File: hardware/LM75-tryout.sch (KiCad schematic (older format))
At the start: 4 parts, among them J1 LM75_HEADER, U1 LM75

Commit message: update,
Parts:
- added JP1: EN, Jumper:SolderJumper-2_P1.3mm_Open_RoundedPad1.0x1.5mm, symbol Jumper:SolderJumper_2_Open
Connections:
- net +3V3: now also JP1.1 (A); no longer C1.1, RN1.6 (R3.2), RN1.7 (R2.2), RN1.8 (R1.2), U1.8 (VCC)
- new net: C1.1, JP1.2 (B), RN1.6 (R3.2), RN1.7 (R2.2), RN1.8 (R1.2), U1.8 (VCC)
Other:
- moved on the sheet: C1, J1, RN1, U1
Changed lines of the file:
@@
 EESchema Schematic File Version 4
+LIBS:LM75-tryout-cache
 EELAYER 29 0
 EELAYER END
@@
 L taobao-components:LM75 U1
 U 1 1 5CEF6143
-P 3000 2000
-F 0 "U1" H 3000 2450 50  0000 C CNN
-F 1 "LM75" H 3000 2350 50  0000 C CNN
-F 2 "Package_SO:SOP-8_3.76x4.96mm_P1.27mm" H 3000 1400 50  0001 C CNN
-F 3 "" H 3000 2000 50  0001 C CNN
-	1    3000 2000
+P 3850 2650
+F 0 "U1" H 3850 3100 50  0000 C CNN
+F 1 "LM75" H 3850 3000 50  0000 C CNN
+F 2 "Package_SO:SOP-8_3.76x4.96mm_P1.27mm" H 3850 2050 50  0001 C CNN
+F 3 "" H 3850 2650 50  0001 C CNN
+	1    3850 2650
 	1    0    0    -1
 $EndComp
@@
 L taobao-rpack:RN_472,0603 RN1
 U 1 1 5CEF7694
-P 2000 1450
-F 0 "RN1" H 2200 1500 50  0000 L CNN
-F 1 "RN_472,0603" H 2200 1450 50  0000 L CNN
-F 2 "Resistor_SMD:R_Array_Concave_4x0603" V 2275 1450 50  0001 C CNN
-F 3 "~" H 2000 1450 50  0001 C CNN
-	1    2000 1450
+P 2850 2100
+F 0 "RN1" H 3050 2150 50  0000 L CNN
+F 1 "RN_472,0603" H 3050 2100 50  0000 L CNN
+F 2 "Resistor_SMD:R_Array_Concave_4x0603" V 3125 2100 50  0001 C CNN
+F 3 "~" H 2850 2100 50  0001 C CNN
+	1    2850 2100
 	1    0    0    -1
 $EndComp
@@
 L taobao-c:C103,0603 C1
 U 1 1 5CEF7ED4
-P 4050 1450
-F 0 "C1" H 4150 1500 50  0000 L CNN
-F 1 "C103,0603" H 4150 1450 50  0000 L CNN
-F 2 "Capacitor_SMD:C_0603_1608Metric_Pad1.05x0.95mm_HandSolder" H 4050 1450 50  0001 C CNN
-F 3 "~" H 4050 1450 50  0001 C CNN
-	1    4050 1450
+P 4900 2100
+F 0 "C1" H 5000 2150 50  0000 L CNN
+F 1 "C103,0603" H 5000 2100 50  0000 L CNN
+F 2 "Capacitor_SMD:C_0603_1608Metric_Pad1.05x0.95mm_HandSolder" H 4900 2100 50  0001 C CNN
+F 3 "~" H 4900 2100 50  0001 C CNN
+	1    4900 2100
 	1    0    0    -1
 $EndComp
@@
 L power:GND #PWR0101
 U 1 1 5CEF86F3
-P 3650 2350
-F 0 "#PWR0101" H 3650 2100 50  0001 C CNN
-F 1 "GND" H 3700 2150 50  0000 C CNN
-F 2 "" H 3650 2350 50  0001 C CNN
-F 3 "" H 3650 2350 50  0001 C CNN
-	1    3650 2350
+P 4500 3000
+F 0 "#PWR0101" H 4500 2750 50  0001 C CNN
+F 1 "GND" H 4550 2800 50  0000 C CNN
+F 2 "" H 4500 3000 50  0001 C CNN
+F 3 "" H 4500 3000 50  0001 C CNN
+	1    4500 3000
 	1    0    0    -1
 $EndComp
 Wire Wire Line
-	3400 1950 3650 1950
+	4250 2600 4500 2600
 Wire Wire Line
-	3650 1950 3650 2050
+	4500 2600 4500 2700
 Wire Wire Line
-	3400 2050 3650 2050
-Connection ~ 3650 2050
+	4250 2700 4500 2700
+Connection ~ 4500 2700
 Wire Wire Line
-	3650 2050 3650 2150
+	4500 2700 4500 2800
 Wire Wire Line
-	3400 2150 3650 2150
-Connection ~ 3650 2150
+	4250 2800 4500 2800
+Connection ~ 4500 2800
 Wire Wire Line
-	3650 2150 3650 2350
+	4500 2800 4500 3000
 $Comp
 L power:GND #PWR0102
 U 1 1 5CEF9E27
-P 4050 1700
-F 0 "#PWR0102" H 4050 1450 50  0001 C CNN
-F 1 "GND" H 4100 1500 50  0000 C CNN
-F 2 "" H 4050 1700 50  0001 C CNN
-F 3 "" H 4050 1700 50  0001 C CNN
-	1    4050 1700
+P 4900 2350
+F 0 "#PWR0102" H 4900 2100 50  0001 C CNN
+F 1 "GND" H 4950 2150 50  0000 C CNN
+F 2 "" H 4900 2350 50  0001 C CNN
+F 3 "" H 4900 2350 50  0001 C CNN
+	1    4900 2350
 	1    0    0    -1
 $EndComp
 Wire Wire Line
-	4050 1550 4050 1700
+	4900 2200 4900 2350
 $Comp
 L power:+3V3 #PWR0103
 U 1 1 5CEFBBD2
-P 3350 1050
-F 0 "#PWR0103" H 3350 900 50  0001 C CNN
-F 1 "+3V3" H 3400 1250 50  0000 C CNN
-F 2 "" H 3350 1050 50  0001 C CNN
-F 3 "" H 3350 1050 50  0001 C CNN
-	1    3350 1050
+P 4200 1200
+F 0 "#PWR0103" H 4200 1050 50  0001 C CNN
+F 1 "+3V3" H 4250 1400 50  0000 C CNN
+F 2 "" H 4200 1200 50  0001 C CNN
+F 3 "" H 4200 1200 50  0001 C CNN
+	1    4200 1200
 	1    0    0    -1
 $EndComp
 Wire Wire Line
-	1800 1100 1800 1250
+	2650 1750 2650 1900
 Wire Wire Line
-	1800 1100 1900 1100
+	2650 1750 2750 1750
 Wire Wire Line
-	3350 1050 3350 1100
+	2750 1900 2750 1750
+Connection ~ 2750 1750
 Wire Wire Line
-	1900 1250 1900 1100
-Connection ~ 1900 1100
+	2750 1750 2850 1750
 Wire Wire Line
-	1900 1100 2000 1100
+	2850 1750 2850 1900
+Connection ~ 2850 1750
 Wire Wire Line
-	2000 1100 2000 1250
-Connection ~ 2000 1100
+	2850 1750 4200 1750
 Wire Wire Line
-	2000 1100 3350 1100
+	4900 2000 4900 1750
+Connection ~ 4200 1750
 Wire Wire Line
-	4050 1350 4050 1100
-Connection ~ 3350 1100
+	4200 1750 4400 1750
 Wire Wire Line
-	3350 1100 3550 1100
+	4250 2500 4400 2500
 Wire Wire Line
-	3400 1850 3550 1850
+	4400 2500 4400 1750
+Connection ~ 4400 1750
 Wire Wire Line
-	3550 1850 3550 1100
-Connection ~ 3550 1100
+	4400 1750 4900 1750
 Wire Wire Line
-	3550 1100 4050 1100
+	3450 2500 2650 2500
 Wire Wire Line
-	2600 1850 1800 1850
+	2650 2300 2650 2500
+Connection ~ 2650 2500
 Wire Wire Line
-	1800 1650 1800 1850
-Connection ~ 1800 1850
+	2650 2500 1800 2500
 Wire Wire Line
-	1800 1850 950  1850
+	1800 2600 2750 2600
 Wire Wire Line
-	950  1950 1900 1950
+	2750 2300 2750 2600
+Connection ~ 2750 2600
 Wire Wire Line
-	1900 1650 1900 1950
-Connection ~ 1900 1950
+	2750 2600 3450 2600
 Wire Wire Line
-	1900 1950 2600 1950
+	1800 2700 2850 2700
 Wire Wire Line
-	950  2050 2000 2050
+	2850 2300 2850 2700
+Connection ~ 2850 2700
 Wire Wire Line
-	2000 1650 2000 2050
-Connection ~ 2000 2050
-Wire Wire Line
-	2000 2050 2600 2050
+	2850 2700 3450 2700
 $Comp
 L power:GND #PWR0104
 U 1 1 5CF0201D
-P 2500 2350
-F 0 "#PWR0104" H 2500 2100 50  0001 C CNN
-F 1 "GND" H 2550 2150 50  0000 C CNN
-F 2 "" H 2500 2350 50  0001 C CNN
-F 3 "" H 2500 2350 50  0001 C CNN
-	1    2500 2350
+P 3350 3000
+F 0 "#PWR0104" H 3350 2750 50  0001 C CNN
+F 1 "GND" H 3400 2800 50  0000 C CNN
+F 2 "" H 3350 3000 50  0001 C CNN
+F 3 "" H 3350 3000 50  0001 C CNN
+	1    3350 3000
 	1    0    0    -1
 $EndComp
 Wire Wire Line
-	2500 2350 2500 2150
+	3350 3000 3350 2800
 Wire Wire Line
-	2500 2150 2600 2150
+	3350 2800 3450 2800
 $Comp
 L Connector:Conn_01x05_Female J1
 U 1 1 5CF06FB7
-P 750 1850
-F 0 "J1" H 600 2250 50  0000 C CNN
-F 1 "LM75_HEADER" H 600 2150 50  0000 C CNN
-F 2 "Connector_PinHeader_1.27mm:PinHeader_1x05_P1.27mm_Vertical" H 750 1850 50  0001 C CNN
-F 3 "~" H 750 1850 50  0001 C CNN
-	1    750  1850
+P 1600 2500
+F 0 "J1" H 1450 2900 50  0000 C CNN
+F 1 "LM75_HEADER" H 1450 2800 50  0000 C CNN
+F 2 "Connector_PinHeader_1.27mm:PinHeader_1x05_P1.27mm_Vertical" H 1600 2500 50  0001 C CNN
+F 3 "~" H 1600 2500 50  0001 C CNN
+	1    1600 2500
 	-1   0    0    -1
 $EndComp
@@
 L power:+3V3 #PWR0105
 U 1 1 5CF08014
-P 1200 1450
-F 0 "#PWR0105" H 1200 1300 50  0001 C CNN
-F 1 "+3V3" H 1250 1650 50  0000 C CNN
-F 2 "" H 1200 1450 50  0001 C CNN
-F 3 "" H 1200 1450 50  0001 C CNN
-	1    1200 1450
+P 2050 2100
+F 0 "#PWR0105" H 2050 1950 50  0001 C CNN
+F 1 "+3V3" H 2100 2300 50  0000 C CNN
+F 2 "" H 2050 2100 50  0001 C CNN
+F 3 "" H 2050 2100 50  0001 C CNN
+	1    2050 2100
 	1    0    0    -1
 $EndComp
@@
 L power:GND #PWR0106
 U 1 1 5CF08421
-P 1350 1500
-F 0 "#PWR0106" H 1350 1250 50  0001 C CNN
-F 1 "GND" H 1400 1300 50  0000 C CNN
-F 2 "" H 1350 1500 50  0001 C CNN
-F 3 "" H 1350 1500 50  0001 C CNN
-	1    1350 1500
+P 2200 2150
+F 0 "#PWR0106" H 2200 1900 50  0001 C CNN
+F 1 "GND" H 2250 1950 50  0000 C CNN
+F 2 "" H 2200 2150 50  0001 C CNN
+F 3 "" H 2200 2150 50  0001 C CNN
+	1    2200 2150
 	-1   0    0    1
 $EndComp
 Wire Wire Line
-	950  1650 1200 1650
+	1800 2300 2050 2300
+Wire Wire Line
+	2050 2300 2050 2100
+Wire Wire Line
+	1800 2400 2200 2400
 Wire Wire Line
-	1200 1650 1200 1450
+	2200 2400 2200 2150
+$Comp
+L Jumper:SolderJumper_2_Open JP1
+U 1 1 5CF0F377
+P 4200 1450
+F 0 "JP1" V 4154 1518 50  0000 L CNN
+F 1 "EN" V 4245 1518 50  0000 L CNN
+F 2 "Jumper:SolderJumper-2_P1.3mm_Open_RoundedPad1.0x1.5mm" H 4200 1450 50  0001 C CNN
+F 3 "~" H 4200 1450 50  0001 C CNN
+	1    4200 1450
+	0    1    1    0
+$EndComp
 Wire Wire Line
-	950  1750 1350 1750
+	4200 1200 4200 1300
 Wire Wire Line
-	1350 1750 1350 1500
+	4200 1600 4200 1750
 $EndSCHEMATC

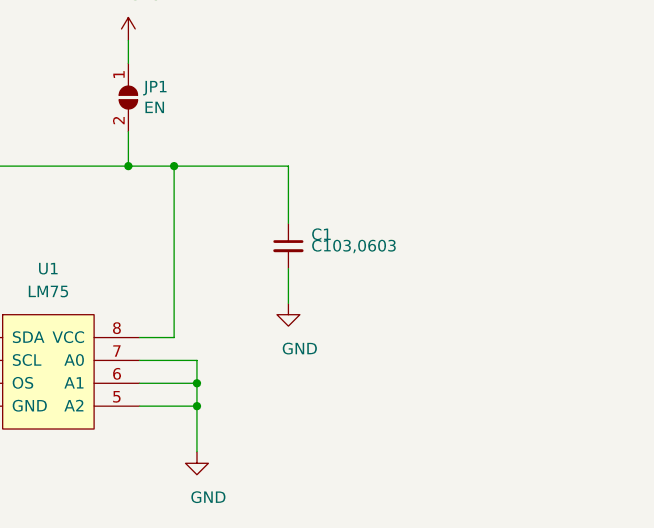
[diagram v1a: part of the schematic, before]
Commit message: update for power led,
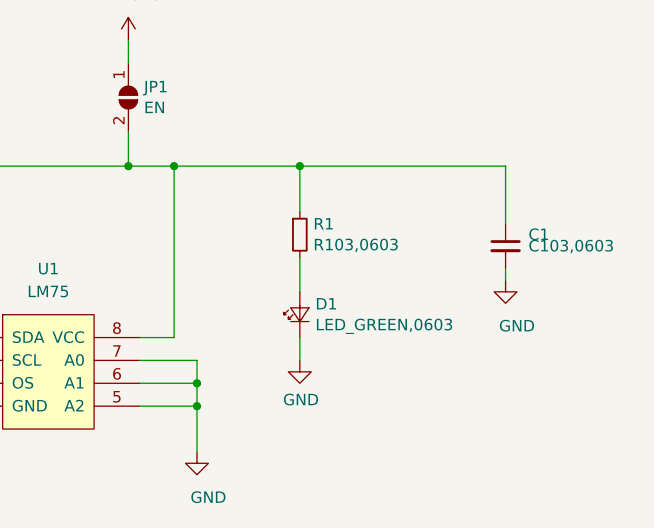
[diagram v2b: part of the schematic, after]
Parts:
- added D1: LED_GREEN,0603, footprint-lib:LED_0603_1608Metric, symbol taobao-led:LED_GREEN,0603
- added R1: R103,0603, Resistor_SMD:R_0603_1608Metric_Pad1.05x0.95mm_HandSolder, symbol taobao-r:R103,0603
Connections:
- net GND: now also D1.1 (K)
- net at C1.1, JP1.2 (B), RN1.6 (R3.2)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: now also R1.1
- new net: D1.2 (A), R1.2
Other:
- moved on the sheet: C1
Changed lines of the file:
@@
 L taobao-c:C103,0603 C1
 U 1 1 5CEF7ED4
-P 4900 2100
-F 0 "C1" H 5000 2150 50  0000 L CNN
-F 1 "C103,0603" H 5000 2100 50  0000 L CNN
-F 2 "Capacitor_SMD:C_0603_1608Metric_Pad1.05x0.95mm_HandSolder" H 4900 2100 50  0001 C CNN
-F 3 "~" H 4900 2100 50  0001 C CNN
-	1    4900 2100
+P 5850 2100
+F 0 "C1" H 5950 2150 50  0000 L CNN
+F 1 "C103,0603" H 5950 2100 50  0000 L CNN
+F 2 "Capacitor_SMD:C_0603_1608Metric_Pad1.05x0.95mm_HandSolder" H 5850 2100 50  0001 C CNN
+F 3 "~" H 5850 2100 50  0001 C CNN
+	1    5850 2100
 	1    0    0    -1
 $EndComp
@@
 L power:GND #PWR0102
 U 1 1 5CEF9E27
-P 4900 2350
-F 0 "#PWR0102" H 4900 2100 50  0001 C CNN
-F 1 "GND" H 4950 2150 50  0000 C CNN
-F 2 "" H 4900 2350 50  0001 C CNN
-F 3 "" H 4900 2350 50  0001 C CNN
-	1    4900 2350
-	1    0    0    -1
-$EndComp
-Wire Wire Line
-	4900 2200 4900 2350
+P 5850 2250
+F 0 "#PWR0102" H 5850 2000 50  0001 C CNN
+F 1 "GND" H 5900 2050 50  0000 C CNN
+F 2 "" H 5850 2250 50  0001 C CNN
+F 3 "" H 5850 2250 50  0001 C CNN
+	1    5850 2250
+	1    0    0    -1
+$EndComp
+Wire Wire Line
+	5850 2200 5850 2250
 $Comp
 L power:+3V3 #PWR0103
@@
 	2850 1750 4200 1750
 Wire Wire Line
-	4900 2000 4900 1750
+	5850 2000 5850 1750
 Connection ~ 4200 1750
 Wire Wire Line
@@
 Connection ~ 4400 1750
 Wire Wire Line
-	4400 1750 4900 1750
+	4400 1750 4950 1750
 Wire Wire Line
 	3450 2500 2650 2500
@@
 Wire Wire Line
 	4200 1600 4200 1750
+$Comp
+L taobao-r:R103,0603 R1
+U 1 1 5CF91DE7
+P 4950 2050
+F 0 "R1" H 5009 2096 50  0000 L CNN
+F 1 "R103,0603" H 5009 2005 50  0000 L CNN
+F 2 "Resistor_SMD:R_0603_1608Metric_Pad1.05x0.95mm_HandSolder" H 4950 2050 50  0001 C CNN
+F 3 "~" H 4950 2050 50  0001 C CNN
+	1    4950 2050
+	1    0    0    -1
+$EndComp
+$Comp
+L taobao-led:LED_GREEN,0603 D1
+U 1 1 5CF92257
+P 4950 2400
+F 0 "D1" V 4996 2332 50  0000 R CNN
+F 1 "LED_GREEN,0603" V 4905 2332 50  0000 R CNN
+F 2 "footprint-lib:LED_0603_1608Metric" V 4950 2400 50  0001 C CNN
+F 3 "" V 4950 2400 50  0001 C CNN
+	1    4950 2400
+	0    -1   -1   0
+$EndComp
+$Comp
+L power:GND #PWR01
+U 1 1 5CF92991
+P 4950 2600
+F 0 "#PWR01" H 4950 2350 50  0001 C CNN
+F 1 "GND" H 4955 2427 50  0000 C CNN
+F 2 "" H 4950 2600 50  0001 C CNN
+F 3 "" H 4950 2600 50  0001 C CNN
+	1    4950 2600
+	1    0    0    -1
+$EndComp
+Wire Wire Line
+	4950 2500 4950 2600
+Wire Wire Line
+	4950 2150 4950 2300
+Wire Wire Line
+	4950 1950 4950 1750
+Connection ~ 4950 1750
+Wire Wire Line
+	4950 1750 5850 1750
 $EndSCHEMATC
